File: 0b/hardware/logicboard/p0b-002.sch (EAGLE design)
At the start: 30 parts, among them IC1 7404D, IC4 LTC485S, IC5 LTC485S, J0 DC5V, J7 DIN5, J9 DIN5, X7 NELTRON-7810-XPXC

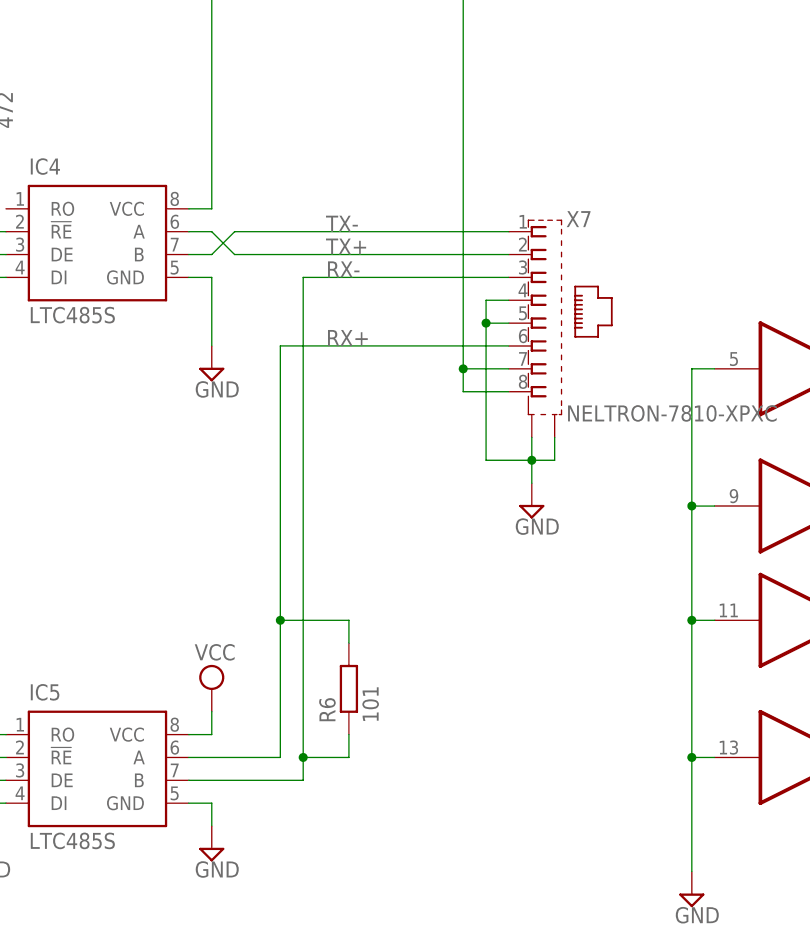
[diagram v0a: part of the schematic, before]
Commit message: Now 0b are divided in type a (straight) and type b (cross).
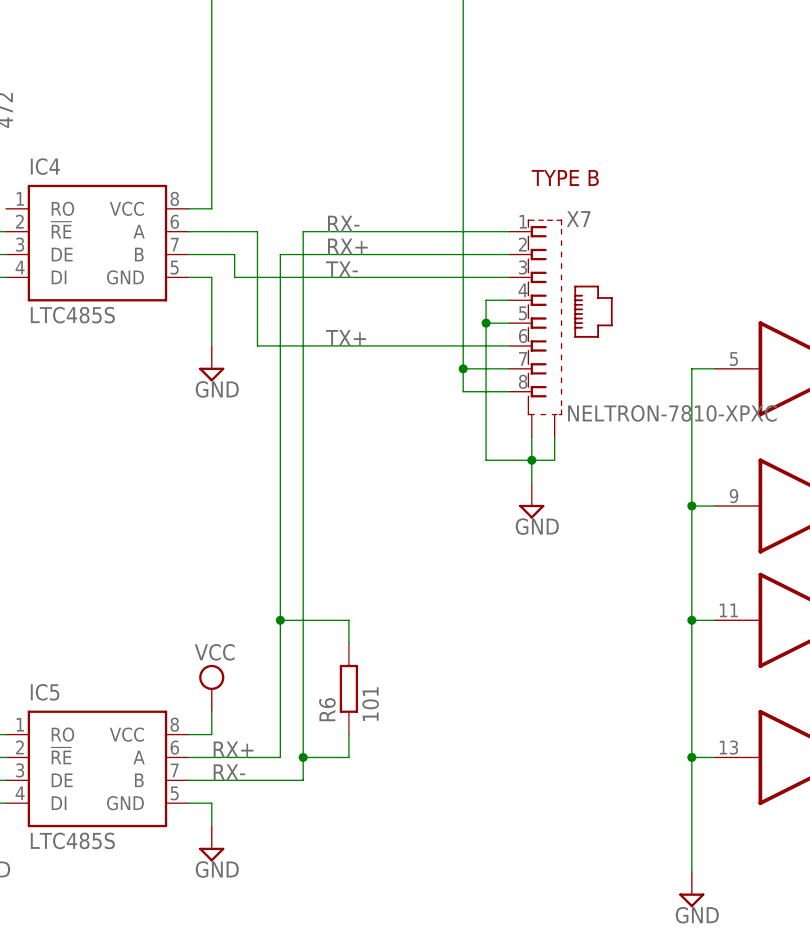
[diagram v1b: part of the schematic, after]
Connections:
- net RX+: now also X7.2; no longer X7.6
- net RX-: now also X7.1; no longer X7.3
- net TX+: now also X7.6; no longer X7.2
- net TX-: now also X7.3; no longer X7.1
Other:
- note added: "TYPE B"
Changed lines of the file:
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@@
 <text x="35.56" y="104.14" size="1.778" layer="94">MIDI IN</text>
 <text x="35.56" y="53.34" size="1.778" layer="94">MIDI OUT</text>
+<text x="203.2" y="124.46" size="1.778" layer="94">TYPE B</text>
 </plain>
 <instances>
@@
 <net name="TX+" class="0">
 <segment>
-<wire x1="165.1" y1="119.38" x2="167.64" y2="119.38" width="0.1524" layer="91"/>
-<wire x1="167.64" y1="119.38" x2="170.18" y2="116.84" width="0.1524" layer="91"/>
-<pinref part="X7" gate="G$1" pin="2"/>
-<wire x1="170.18" y1="116.84" x2="200.66" y2="116.84" width="0.1524" layer="91"/>
-<label x="180.34" y="116.84" size="1.778" layer="95"/>
 <pinref part="IC4" gate="G$1" pin="A"/>
-</segment>
-</net>
-<net name="TX-" class="0">
-<segment>
-<pinref part="X7" gate="G$1" pin="1"/>
-<wire x1="200.66" y1="119.38" x2="170.18" y2="119.38" width="0.1524" layer="91"/>
-<wire x1="170.18" y1="119.38" x2="167.64" y2="116.84" width="0.1524" layer="91"/>
-<wire x1="167.64" y1="116.84" x2="165.1" y2="116.84" width="0.1524" layer="91"/>
-<label x="180.34" y="119.38" size="1.778" layer="95"/>
-<pinref part="IC4" gate="G$1" pin="B"/>
+<wire x1="165.1" y1="119.38" x2="172.72" y2="119.38" width="0.1524" layer="91"/>
+<wire x1="172.72" y1="119.38" x2="172.72" y2="106.68" width="0.1524" layer="91"/>
+<pinref part="X7" gate="G$1" pin="6"/>
+<wire x1="172.72" y1="106.68" x2="200.66" y2="106.68" width="0.1524" layer="91"/>
+<label x="180.34" y="106.68" size="1.778" layer="95"/>
 </segment>
 </net>
 <net name="RX+" class="0">
 <segment>
-<pinref part="X7" gate="G$1" pin="6"/>
 <wire x1="165.1" y1="60.96" x2="175.26" y2="60.96" width="0.1524" layer="91"/>
-<label x="180.34" y="106.68" size="1.778" layer="95"/>
-<wire x1="200.66" y1="106.68" x2="175.26" y2="106.68" width="0.1524" layer="91"/>
-<wire x1="175.26" y1="106.68" x2="175.26" y2="76.2" width="0.1524" layer="91"/>
+<label x="167.64" y="60.96" size="1.778" layer="95"/>
+<wire x1="175.26" y1="116.84" x2="175.26" y2="76.2" width="0.1524" layer="91"/>
 <wire x1="175.26" y1="76.2" x2="175.26" y2="60.96" width="0.1524" layer="91"/>
 <wire x1="175.26" y1="76.2" x2="182.88" y2="76.2" width="0.1524" layer="91"/>
@@
 <pinref part="IC5" gate="G$1" pin="A"/>
 <pinref part="R6" gate="G$1" pin="2"/>
+<pinref part="X7" gate="G$1" pin="2"/>
+<wire x1="200.66" y1="116.84" x2="175.26" y2="116.84" width="0.1524" layer="91"/>
+<label x="180.34" y="116.84" size="1.778" layer="95"/>
 </segment>
 </net>
 <net name="RX-" class="0">
 <segment>
-<pinref part="X7" gate="G$1" pin="3"/>
-<wire x1="200.66" y1="114.3" x2="177.8" y2="114.3" width="0.1524" layer="91"/>
-<wire x1="177.8" y1="114.3" x2="177.8" y2="60.96" width="0.1524" layer="91"/>
+<wire x1="177.8" y1="119.38" x2="177.8" y2="60.96" width="0.1524" layer="91"/>
 <wire x1="177.8" y1="60.96" x2="177.8" y2="58.42" width="0.1524" layer="91"/>
 <wire x1="177.8" y1="58.42" x2="165.1" y2="58.42" width="0.1524" layer="91"/>
-<label x="180.34" y="114.3" size="1.778" layer="95"/>
+<label x="167.64" y="58.42" size="1.778" layer="95"/>
 <wire x1="182.88" y1="63.5" x2="182.88" y2="60.96" width="0.1524" layer="91"/>
 <wire x1="182.88" y1="60.96" x2="177.8" y2="60.96" width="0.1524" layer="91"/>
@@
 <pinref part="IC5" gate="G$1" pin="B"/>
 <pinref part="R6" gate="G$1" pin="1"/>
+<pinref part="X7" gate="G$1" pin="1"/>
+<wire x1="200.66" y1="119.38" x2="177.8" y2="119.38" width="0.1524" layer="91"/>
+<label x="180.34" y="119.38" size="1.778" layer="95"/>
 </segment>
 </net>
@@
 </segment>
 </net>
+<net name="TX-" class="0">
+<segment>
+<pinref part="IC4" gate="G$1" pin="B"/>
+<pinref part="X7" gate="G$1" pin="3"/>
+<wire x1="200.66" y1="114.3" x2="170.18" y2="114.3" width="0.1524" layer="91"/>
+<wire x1="170.18" y1="114.3" x2="170.18" y2="116.84" width="0.1524" layer="91"/>
+<wire x1="170.18" y1="116.84" x2="165.1" y2="116.84" width="0.1524" layer="91"/>
+<label x="180.34" y="114.3" size="1.778" layer="95"/>
+</segment>
+</net>
